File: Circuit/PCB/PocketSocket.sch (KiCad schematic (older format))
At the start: 12 parts, among them P1 CONN_02X25, P2 UART, P3 I2C, U1 CY8CKIT-059_Target, Y1 24.576M, Y2 32.768k

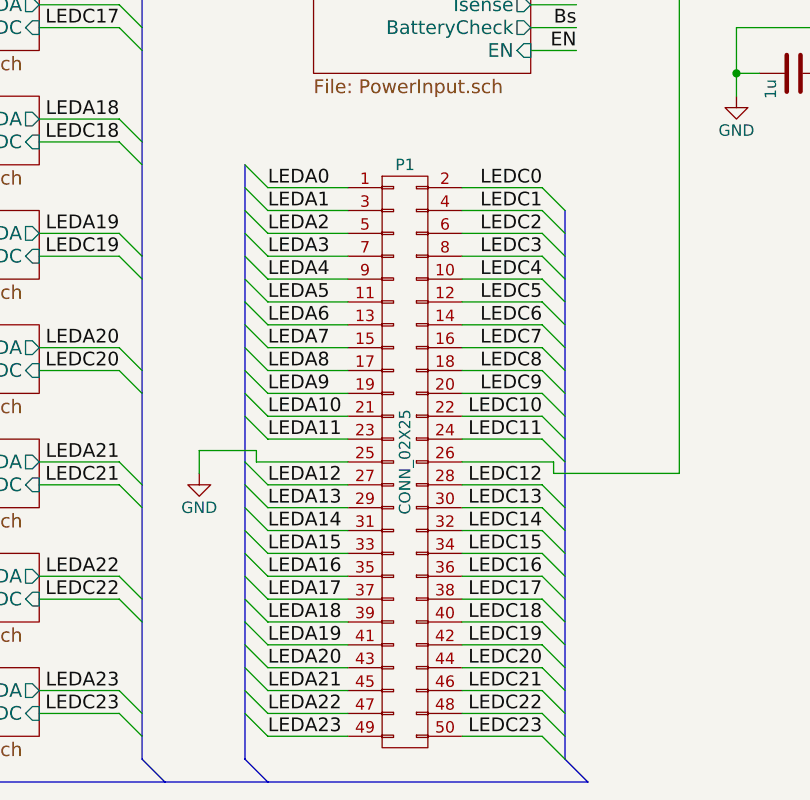
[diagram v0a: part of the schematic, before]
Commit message: CvPcb settled
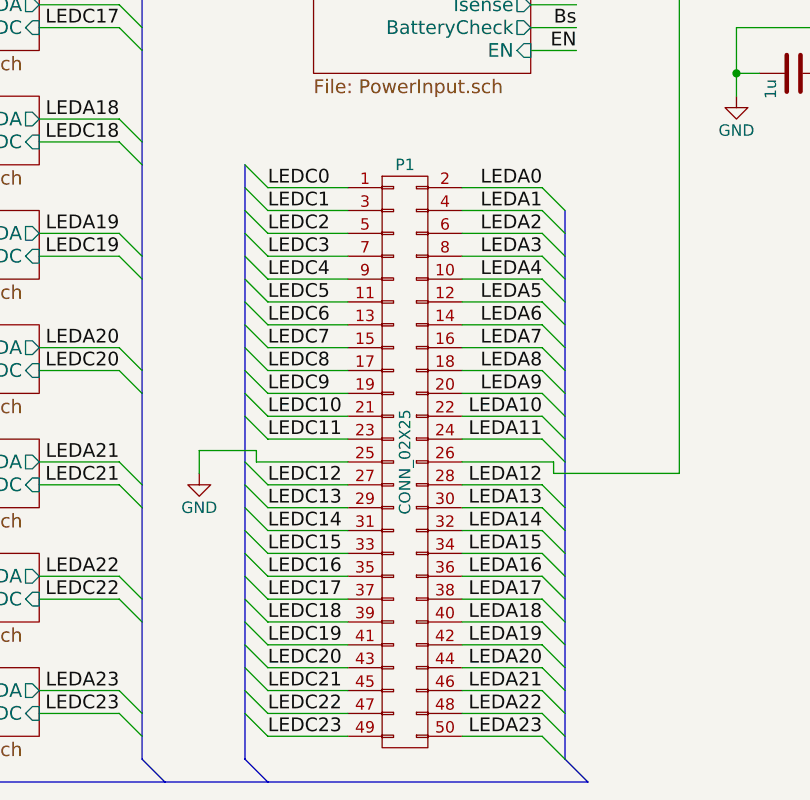
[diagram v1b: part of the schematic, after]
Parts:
- P1: footprint (none) -> conn:DF50-50DP-1H
- U1: footprint (none) -> uC:CY8KIT-059_Target
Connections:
- net LEDA0: now also P1.2 (P2); no longer P1.1 (P1)
- net LEDA1: now also P1.4 (P4); no longer P1.3 (P3)
- net LEDA10: now also P1.22 (P22); no longer P1.21 (P21)
- net LEDA11: now also P1.24 (P24); no longer P1.23 (P23)
- net LEDA12: now also P1.28 (P28); no longer P1.27 (P27)
- net LEDA13: now also P1.30 (P30); no longer P1.29 (P29)
- net LEDA14: now also P1.32 (P32); no longer P1.31 (P31)
- net LEDA15: now also P1.34 (P34); no longer P1.33 (P33)
- net LEDA16: now also P1.36 (P36); no longer P1.35 (P35)
- net LEDA17: now also P1.38 (P38); no longer P1.37 (P37)
- net LEDA18: now also P1.40 (P40); no longer P1.39 (P39)
- net LEDA19: now also P1.42 (P42); no longer P1.41 (P41)
- net LEDA2: now also P1.6 (P6); no longer P1.5 (P5)
- net LEDA20: now also P1.44 (P44); no longer P1.43 (P43)
- net LEDA21: now also P1.46 (P46); no longer P1.45 (P45)
- net LEDA22: now also P1.48 (P48); no longer P1.47 (P47)
- net LEDA23: now also P1.50 (P50); no longer P1.49 (P49)
- net LEDA3: now also P1.8 (P8); no longer P1.7 (P7)
- net LEDA4: now also P1.10 (P10); no longer P1.9 (P9)
- net LEDA5: now also P1.12 (P12); no longer P1.11 (P11)
- net LEDA6: now also P1.14 (P14); no longer P1.13 (P13)
- net LEDA7: now also P1.16 (P16); no longer P1.15 (P15)
- net LEDA8: now also P1.18 (P18); no longer P1.17 (P17)
- net LEDA9: now also P1.20 (P20); no longer P1.19 (P19)
- net LEDC0: now also P1.1 (P1); no longer P1.2 (P2)
- net LEDC1: now also P1.3 (P3); no longer P1.4 (P4)
- net LEDC10: now also P1.21 (P21); no longer P1.22 (P22)
- net LEDC11: now also P1.23 (P23); no longer P1.24 (P24)
- net LEDC12: now also P1.27 (P27); no longer P1.28 (P28)
- net LEDC13: now also P1.29 (P29); no longer P1.30 (P30)
- net LEDC14: now also P1.31 (P31); no longer P1.32 (P32)
- net LEDC15: now also P1.33 (P33); no longer P1.34 (P34)
- net LEDC16: now also P1.35 (P35); no longer P1.36 (P36)
- net LEDC17: now also P1.37 (P37); no longer P1.38 (P38)
- net LEDC18: now also P1.39 (P39); no longer P1.40 (P40)
- net LEDC19: now also P1.41 (P41); no longer P1.42 (P42)
- net LEDC2: now also P1.5 (P5); no longer P1.6 (P6)
- net LEDC20: now also P1.43 (P43); no longer P1.44 (P44)
- net LEDC21: now also P1.45 (P45); no longer P1.46 (P46)
- net LEDC22: now also P1.47 (P47); no longer P1.48 (P48)
- net LEDC23: now also P1.49 (P49); no longer P1.50 (P50)
- net LEDC3: now also P1.7 (P7); no longer P1.8 (P8)
- net LEDC4: now also P1.9 (P9); no longer P1.10 (P10)
- net LEDC5: now also P1.11 (P11); no longer P1.12 (P12)
- net LEDC6: now also P1.13 (P13); no longer P1.14 (P14)
- net LEDC7: now also P1.15 (P15); no longer P1.16 (P16)
- net LEDC8: now also P1.17 (P17); no longer P1.18 (P18)
- net LEDC9: now also P1.19 (P19); no longer P1.20 (P20)
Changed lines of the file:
@@
 F 0 "U1" H 8450 4600 60  0000 C CNN
 F 1 "CY8CKIT-059_Target" H 8450 1900 60  0000 C CNN
-F 2 "" H 8150 4500 60  0001 C CNN
+F 2 "uC:CY8KIT-059_Target" H 8150 4500 60  0001 C CNN
 F 3 "" H 8150 4500 60  0000 C CNN
 	1    8450 3250
@@
 F 0 "P1" H 5500 7600 50  0000 C CNN
 F 1 "CONN_02X25" V 5500 6300 50  0000 C CNN
-F 2 "" H 5500 5550 60  0001 C CNN
+F 2 "conn:DF50-50DP-1H" H 5500 5550 60  0001 C CNN
 F 3 "" H 5500 5550 60  0000 C CNN
 	1    5500 6300
@@
 	2450 1900 2450 7600
 Text Label 4900 5100 0    60   ~ 0
+LEDC0
+Text Label 4900 5200 0    60   ~ 0
+LEDC1
+Text Label 4900 5300 0    60   ~ 0
+LEDC2
+Text Label 4900 5400 0    60   ~ 0
+LEDC3
+Text Label 4900 5500 0    60   ~ 0
+LEDC4
+Text Label 4900 5600 0    60   ~ 0
+LEDC5
+Text Label 4900 5700 0    60   ~ 0
+LEDC6
+Text Label 4900 5800 0    60   ~ 0
+LEDC7
+Text Label 4900 5900 0    60   ~ 0
+LEDC8
+Text Label 4900 6000 0    60   ~ 0
+LEDC9
+Text Label 4900 6100 0    60   ~ 0
+LEDC10
+Text Label 4900 6200 0    60   ~ 0
+LEDC11
+Text Label 4900 6400 0    60   ~ 0
+LEDC12
+Text Label 4900 6500 0    60   ~ 0
+LEDC13
+Text Label 4900 6600 0    60   ~ 0
+LEDC14
+Text Label 4900 6700 0    60   ~ 0
+LEDC15
+Text Label 4900 6800 0    60   ~ 0
+LEDC16
+Text Label 4900 6900 0    60   ~ 0
+LEDC17
+Text Label 4900 7000 0    60   ~ 0
+LEDC18
+Text Label 4900 7100 0    60   ~ 0
+LEDC19
+Text Label 4900 7200 0    60   ~ 0
+LEDC20
+Text Label 4900 7300 0    60   ~ 0
+LEDC21
+Text Label 4900 7400 0    60   ~ 0
+LEDC22
+Text Label 4900 7500 0    60   ~ 0
+LEDC23
+Text Label 6100 5100 2    60   ~ 0
 LEDA0
-Text Label 4900 5200 0    60   ~ 0
+Text Label 6100 5200 2    60   ~ 0
 LEDA1
-Text Label 4900 5300 0    60   ~ 0
+Text Label 6100 5300 2    60   ~ 0
 LEDA2
-Text Label 4900 5400 0    60   ~ 0
+Text Label 6100 5400 2    60   ~ 0
 LEDA3
-Text Label 4900 5500 0    60   ~ 0
+Text Label 6100 5500 2    60   ~ 0
 LEDA4
-Text Label 4900 5600 0    60   ~ 0
+Text Label 6100 5600 2    60   ~ 0
 LEDA5
-Text Label 4900 5700 0    60   ~ 0
+Text Label 6100 5700 2    60   ~ 0
 LEDA6
-Text Label 4900 5800 0    60   ~ 0
+Text Label 6100 5800 2    60   ~ 0
 LEDA7
-Text Label 4900 5900 0    60   ~ 0
+Text Label 6100 5900 2    60   ~ 0
 LEDA8
-Text Label 4900 6000 0    60   ~ 0
+Text Label 6100 6000 2    60   ~ 0
 LEDA9
-Text Label 4900 6100 0    60   ~ 0
+Text Label 6100 6100 2    60   ~ 0
 LEDA10
-Text Label 4900 6200 0    60   ~ 0
+Text Label 6100 6200 2    60   ~ 0
 LEDA11
-Text Label 4900 6400 0    60   ~ 0
+Text Label 6100 6400 2    60   ~ 0
 LEDA12
-Text Label 4900 6500 0    60   ~ 0
+Text Label 6100 6500 2    60   ~ 0
 LEDA13
-Text Label 4900 6600 0    60   ~ 0
+Text Label 6100 6600 2    60   ~ 0
 LEDA14
-Text Label 4900 6700 0    60   ~ 0
+Text Label 6100 6700 2    60   ~ 0
 LEDA15
-Text Label 4900 6800 0    60   ~ 0
+Text Label 6100 6800 2    60   ~ 0
 LEDA16
-Text Label 4900 6900 0    60   ~ 0
+Text Label 6100 6900 2    60   ~ 0
 LEDA17
-Text Label 4900 7000 0    60   ~ 0
+Text Label 6100 7000 2    60   ~ 0
 LEDA18
-Text Label 4900 7100 0    60   ~ 0
+Text Label 6100 7100 2    60   ~ 0
 LEDA19
-Text Label 4900 7200 0    60   ~ 0
+Text Label 6100 7200 2    60   ~ 0
 LEDA20
-Text Label 4900 7300 0    60   ~ 0
+Text Label 6100 7300 2    60   ~ 0
 LEDA21
-Text Label 4900 7400 0    60   ~ 0
+Text Label 6100 7400 2    60   ~ 0
 LEDA22
-Text Label 4900 7500 0    60   ~ 0
+Text Label 6100 7500 2    60   ~ 0
 LEDA23
-Text Label 6100 5100 2    60   ~ 0
-LEDC0
-Text Label 6100 5200 2    60   ~ 0
-LEDC1
-Text Label 6100 5300 2    60   ~ 0
-LEDC2
-Text Label 6100 5400 2    60   ~ 0
-LEDC3
-Text Label 6100 5500 2    60   ~ 0
-LEDC4
-Text Label 6100 5600 2    60   ~ 0
-LEDC5
-Text Label 6100 5700 2    60   ~ 0
-LEDC6
-Text Label 6100 5800 2    60   ~ 0
-LEDC7
-Text Label 6100 5900 2    60   ~ 0
-LEDC8
-Text Label 6100 6000 2    60   ~ 0
-LEDC9
-Text Label 6100 6100 2    60   ~ 0
-LEDC10
-Text Label 6100 6200 2    60   ~ 0
-LEDC11
-Text Label 6100 6400 2    60   ~ 0
-LEDC12
-Text Label 6100 6500 2    60   ~ 0
-LEDC13
-Text Label 6100 6600 2    60   ~ 0
-LEDC14
-Text Label 6100 6700 2    60   ~ 0
-LEDC15
-Text Label 6100 6800 2    60   ~ 0
-LEDC16
-Text Label 6100 6900 2    60   ~ 0
-LEDC17
-Text Label 6100 7000 2    60   ~ 0
-LEDC18
-Text Label 6100 7100 2    60   ~ 0
-LEDC19
-Text Label 6100 7200 2    60   ~ 0
-LEDC20
-Text Label 6100 7300 2    60   ~ 0
-LEDC21
-Text Label 6100 7400 2    60   ~ 0
-LEDC22
-Text Label 6100 7500 2    60   ~ 0
-LEDC23
 Wire Wire Line
 	4900 5100 5250 5100

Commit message: update pcb
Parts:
- C1, C2: footprint Capacitors_SMD:C_1206_HandSoldering -> Capacitors_SMD:C_1206
- P2, P3: footprint Connect:bornier4 -> conn:B4B-XH-A
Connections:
- net Is: now also U1.21 (P0[5]); no longer U1.22 (P0[6])
- net LED0: now also U1.2 (P3[0]); no longer U1.50 (P1[7])
- net LED1: now also U1.3 (P3[1]); no longer U1.49 (P1[6])
- net LED10: now also U1.48 (P1[5]); no longer U1.34 (P2[7])
- net LED11: now also U1.47 (P1[4]); no longer U1.33 (P2[6])
- net LED12: now also U1.46 (P1[3]); no longer U1.32 (P2[5])
- net LED13: now also U1.46 (P1[3]); no longer U1.31 (P2[4])
- net LED14: now also U1.40 (P12[2]); no longer U1.30 (P2[3])
- net LED15: now also U1.39 (P12[3]); no longer U1.27 (P2[0])
- net LED16: now also U1.38 (P12[4]); no longer U1.2 (P3[0])
- net LED17: now also U1.37 (P12[5]); no longer U1.3 (P3[1])
- net LED18: now also U1.34 (P2[7]); no longer U1.5 (P3[3])
- net LED19: now also U1.33 (P2[6]); no longer U1.6 (P3[4])
- net LED2: now also U1.5 (P3[3]); no longer U1.48 (P1[5])
- net LED20: now also U1.32 (P2[5]); no longer U1.7 (P3[5])
- net LED21: now also U1.31 (P2[4]); no longer U1.8 (P3[6])
- net LED22: now also U1.30 (P2[3]); no longer U1.9 (P3[7])
- net LED23: now also U1.27 (P2[0]); no longer U1.15 (P15[5])
- net LED3: now also U1.6 (P3[4]); no longer U1.47 (P1[4])
- net LED4: now also U1.7 (P3[5]); no longer U1.46 (P1[3])
- net LED5: now also U1.8 (P3[6]); no longer U1.46 (P1[3])
- net LED6: now also U1.9 (P3[7]); no longer U1.40 (P12[2])
- net LED7: now also U1.15 (P15[5]); no longer U1.39 (P12[3])
- net LED8: now also U1.50 (P1[7]); no longer U1.38 (P12[4])
- net LED9: now also U1.49 (P1[6]); no longer U1.37 (P12[5])
- net RX: now also P2.2 (P2); no longer P2.3 (P3)
- net TX: now also P2.3 (P3); no longer P2.2 (P2)
- net Vs: now also U1.22 (P0[6]); no longer U1.21 (P0[5])
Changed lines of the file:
@@
 F 0 "P3" H 9350 5950 50  0000 C CNN
 F 1 "I2C" V 9450 5700 50  0000 C CNN
-F 2 "Connect:bornier4" H 9350 5700 60  0001 C CNN
+F 2 "conn:B4B-XH-A" H 9350 5700 60  0001 C CNN
 F 3 "" H 9350 5700 60  0000 C CNN
 	1    9350 5700
@@
 Entry Bus Bus
 	4350 7600 4450 7700
+Text Label 6950 2100 2    60   ~ 0
+LED0
+Text Label 6950 2200 2    60   ~ 0
+LED1
+Text Label 6900 2400 2    60   ~ 0
+LED2
+Text Label 6900 2500 2    60   ~ 0
+LED3
+Text Label 6900 2600 2    60   ~ 0
+LED4
+Text Label 6900 2700 2    60   ~ 0
+LED5
+Text Label 6900 2800 2    60   ~ 0
+LED6
+Text Label 6900 3400 2    60   ~ 0
+LED7
 Text Label 10200 2200 2    60   ~ 0
-LED0
+LED8
 Text Label 10200 2300 2    60   ~ 0
-LED1
+LED9
 Text Label 10200 2400 2    60   ~ 0
-LED2
+LED10
 Text Label 10200 2500 2    60   ~ 0
-LED3
+LED11
 Text Label 10200 2600 2    60   ~ 0
-LED4
+LED12
 Text Label 10200 2700 2    60   ~ 0
-LED5
+LED13
 Text Label 10200 3200 2    60   ~ 0
-LED6
+LED14
 Text Label 10200 3300 2    60   ~ 0
-LED7
+LED15
 Text Label 10200 3400 2    60   ~ 0
-LED8
+LED16
 Text Label 10200 3500 2    60   ~ 0
-LED9
+LED17
 Text Label 10200 3800 2    60   ~ 0
-LED10
+LED18
 Text Label 10200 3900 2    60   ~ 0
-LED11
+LED19
 Text Label 10200 4000 2    60   ~ 0
-LED12
+LED20
 Text Label 10200 4100 2    60   ~ 0
-LED13
+LED21
 Text Label 10200 4200 2    60   ~ 0
-LED14
+LED22
 Text Label 10200 4500 2    60   ~ 0
-LED15
-Text Label 7000 2100 2    60   ~ 0
-LED16
-Text Label 7000 2200 2    60   ~ 0
-LED17
-Text Label 7000 2400 2    60   ~ 0
-LED18
-Text Label 7000 2500 2    60   ~ 0
-LED19
-Text Label 7000 2600 2    60   ~ 0
-LED20
-Text Label 7000 2700 2    60   ~ 0
-LED21
-Text Label 7000 2800 2    60   ~ 0
-LED22
-Text Label 7000 3400 2    60   ~ 0
 LED23
 Wire Wire Line
@@
 F 0 "P2" H 8200 5950 50  0000 C CNN
 F 1 "UART" V 8300 5700 50  0000 C CNN
-F 2 "Connect:bornier4" H 8200 5700 60  0001 C CNN
+F 2 "conn:B4B-XH-A" H 8200 5700 60  0001 C CNN
 F 3 "" H 8200 5700 60  0000 C CNN
 	1    8200 5700
@@
 	1    0    0    -1
 $EndComp
+Text Label 7750 5750 0    60   ~ 0
+TX
 Text Label 7750 5650 0    60   ~ 0
-TX
-Text Label 7750 5750 0    60   ~ 0
 RX
 $Comp
@@
 	7900 5550 8000 5550
 Wire Wire Line
-	8000 5650 7750 5650
-Wire Wire Line
-	7750 5750 8000 5750
+	8000 5750 7750 5750
+Wire Wire Line
+	7750 5650 8000 5650
 Wire Wire Line
 	8500 5250 8500 5550
@@
 Wire Wire Line
 	9550 3700 9350 3700
+Text Label 7400 4100 0    60   ~ 0
+Vs
 Text Label 7400 4000 0    60   ~ 0
-Vs
-Text Label 7400 4100 0    60   ~ 0
 Is
 Text Label 7400 4200 0    60   ~ 0
@@
 F 0 "C2" H 5875 3450 50  0000 L CNN
 F 1 "12p" H 5875 3250 50  0000 L CNN
-F 2 "Capacitors_SMD:C_1206_HandSoldering" H 5888 3200 30  0001 C CNN
+F 2 "Capacitors_SMD:C_1206" H 5888 3200 30  0001 C CNN
 F 3 "" H 5850 3350 60  0000 C CNN
 	1    5850 3350
@@
 F 0 "C1" H 5375 3450 50  0000 L CNN
 F 1 "12p" H 5375 3250 50  0000 L CNN
-F 2 "Capacitors_SMD:C_1206_HandSoldering" H 5388 3200 30  0001 C CNN
+F 2 "Capacitors_SMD:C_1206" H 5388 3200 30  0001 C CNN
 F 3 "" H 5350 3350 60  0000 C CNN
 	1    5350 3350
